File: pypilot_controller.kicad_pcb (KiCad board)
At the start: 4 copper layers, 76.6 x 50.6 mm, 99 parts, among them J1 power+, J10 Clutch, J2 power-, J3 Motor A, J4 Motor B, J5 UART_Device, J6 Rudder, J7 End Stops, J8 Conn_01x02, J9 ISP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

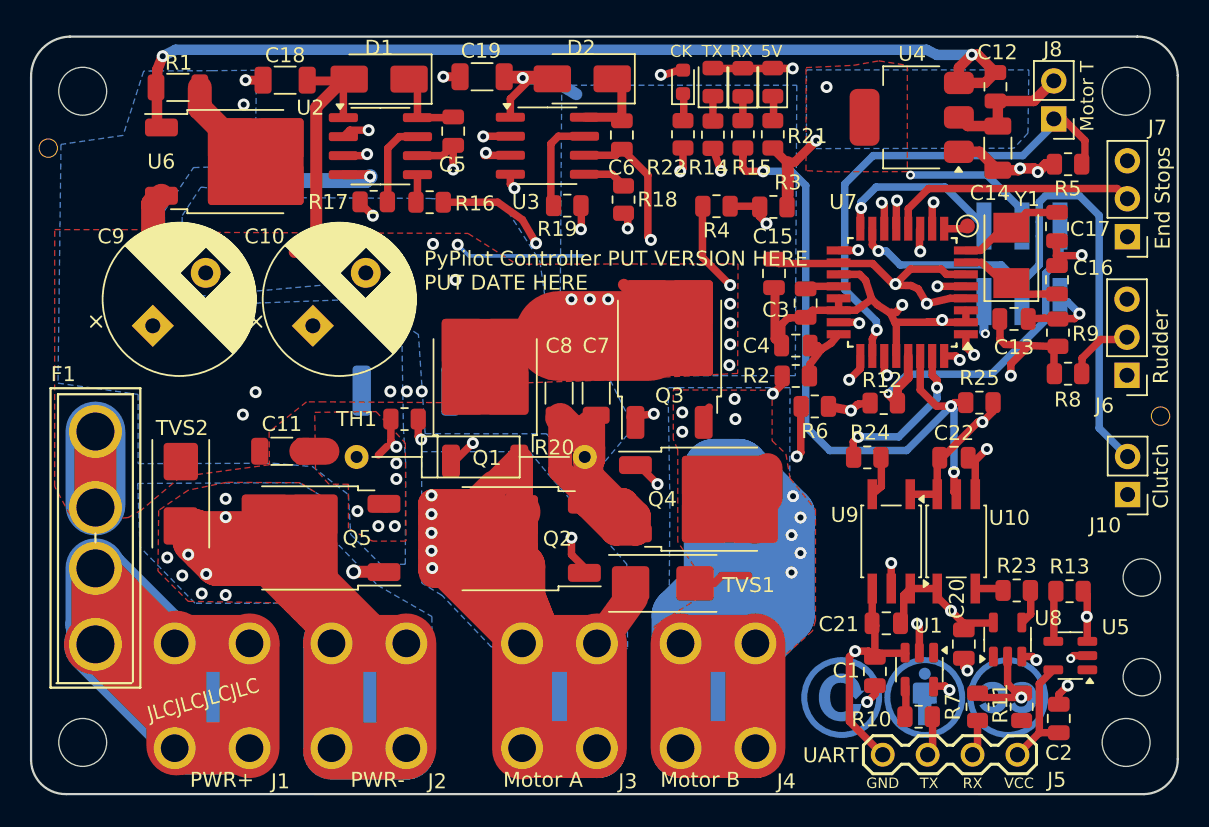
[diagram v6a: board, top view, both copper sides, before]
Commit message: Track cleanups, mostly from Tools -> Cleanup Tracks & Vias
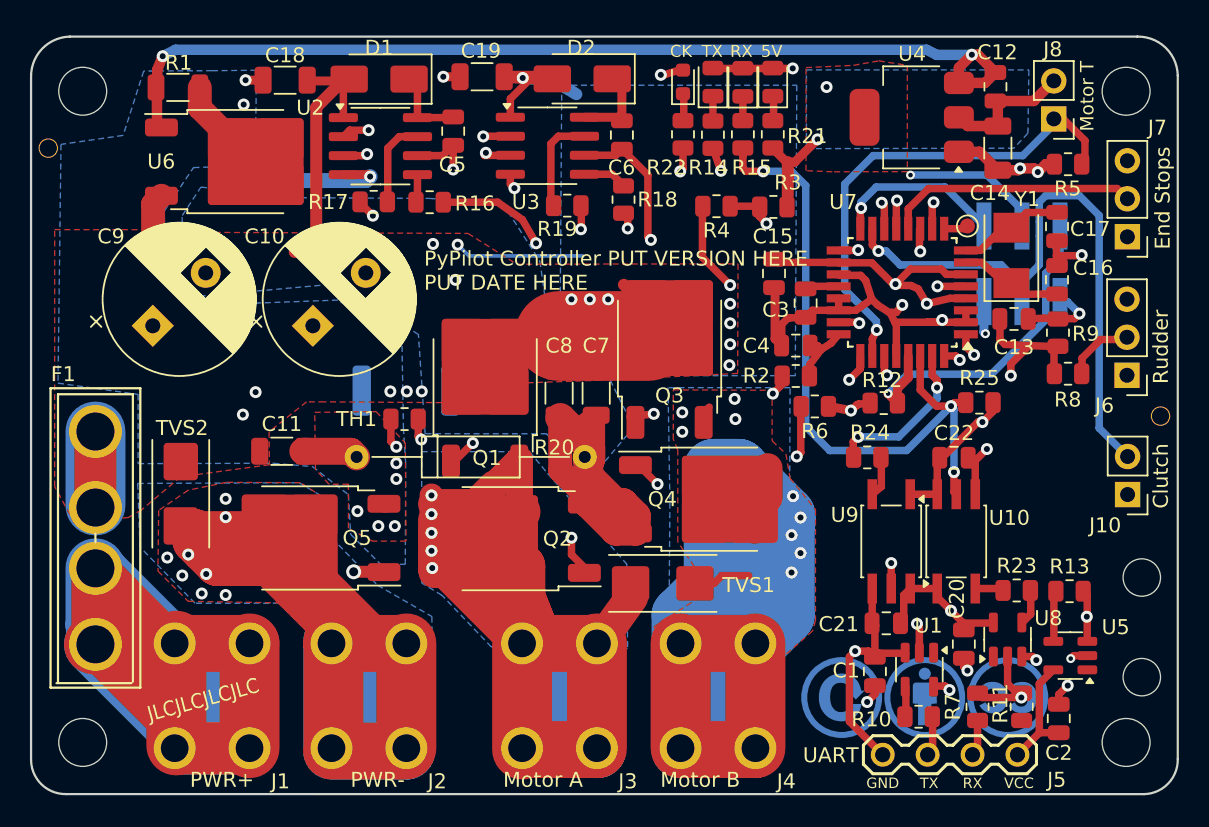
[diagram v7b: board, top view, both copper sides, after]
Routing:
- net Net-(J3-Pin_1): track 162.2 -> 166.1 mm
- net GND: track 82.6 -> 84.1 mm
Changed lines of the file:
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@@
 	)
 	(segment
-		(start 25.618763 28.331237)
-		(end 25.05 28.9)
-		(width 0.5)
-		(layer "F.Cu")
-		(net 1)
-	)
-	(segment
 		(start 55.7974 19.232)
 		(end 55.7974 18.432)
@@
 	)
 	(segment
+		(start 57.2654 16.9)
+		(end 57.5974 17.232)
+		(width 0.5)
+		(layer "F.Cu")
+		(net 1)
+	)
+	(segment
 		(start 51.3988 8.4154)
 		(end 52.3154 9.332)
@@
 	)
 	(segment
-		(start 20 28.65)
-		(end 21.55 28.65)
-		(width 1.8)
-		(layer "F.Cu")
-		(net 1)
-	)
-	(segment
 		(start 69.5198 19.7612)
 		(end 70.4474 19.7889)
@@
 	)
 	(segment
+		(start 23.2166 28.65)
+		(end 23.5966 29.03)
+		(width 1.8)
+		(layer "F.Cu")
+		(net 1)
+	)
+	(segment
 		(start 64.9224 29.2776)
 		(end 65.7 28.5)
@@
 	)
 	(segment
+		(start 52.3154 9.332)
+		(end 52.868 9.332)
+		(width 0.6)
+		(layer "F.Cu")
+		(net 1)
+	)
+	(segment
 		(start 70.3474 14.611)
 		(end 70.3834 14.575)
@@
 	)
 	(segment
+		(start 55.7974 16.832)
+		(end 55.8654 16.9)
+		(width 0.5)
+		(layer "F.Cu")
+		(net 1)
+	)
+	(segment
 		(start 68.8286 5.25)
 		(end 70.1698 3.9088)
@@
 	)
 	(segment
+		(start 55.8654 16.9)
+		(end 57.2654 16.9)
+		(width 0.5)
+		(layer "F.Cu")
+		(net 1)
+	)
+	(segment
 		(start 33.8662 10.1456)
 		(end 33.8662 10.803)
@@
 	)
 	(segment
-		(start 70.3474 16.256)
-		(end 70.3474 15.585)
-		(width 0.5)
+		(start 20 28.65)
+		(end 23.2166 28.65)
+		(width 1.8)
 		(layer "F.Cu")
 		(net 1)
 	)
 	(segment
-		(start 52.3154 9.332)
-		(end 52.868 9.332)
-		(width 0.6)
+		(start 70.3474 16.256)
+		(end 70.3474 15.585)
+		(width 0.5)
 		(layer "F.Cu")
 		(net 1)
@@
 	)
 	(segment
-		(start 52.868 9.332)
-		(end 54.3 7.9)
-		(width 0.6)
-		(layer "F.Cu")
-		(net 1)
-	)
-	(segment
 		(start 33.8662 10.803)
 		(end 34.1376 11.0744)
@@
 	)
 	(segment
-		(start 57.1974 16.832)
-		(end 57.5974 17.232)
-		(width 0.5)
-		(layer "F.Cu")
-		(net 1)
-	)
-	(segment
 		(start 51.9984 20.163)
 		(end 51.9984 21.59)
@@
 	)
 	(segment
-		(start 57.5974 17.232)
-		(end 58.0099 18.4945)
-		(width 0.5)
-		(layer "F.Cu")
-		(net 1)
-	)
-	(segment
 		(start 52.3736 12.2186)
 		(end 52.4002 12.192)
@@
 	)
 	(segment
+		(start 57.5974 17.232)
+		(end 58.0099 18.4945)
+		(width 0.5)
+		(layer "F.Cu")
+		(net 1)
+	)
+	(segment
 		(start 58.3784 18.863)
 		(end 58.0099 18.4945)
@@
 	)
 	(segment
-		(start 55.7974 16.832)
-		(end 57.1974 16.832)
-		(width 0.5)
-		(layer "F.Cu")
-		(net 1)
-	)
-	(segment
 		(start 25.8875 26.5)
 		(end 25.8875 27.9875)
@@
 	)
 	(segment
+		(start 52.868 9.332)
+		(end 54.386397 7.813603)
+		(width 0.6)
+		(layer "F.Cu")
+		(net 1)
+	)
+	(segment
 		(start 52.3974 9.332)
 		(end 52.4002 10.3378)
@@
 	)
 	(via
-		(at 54.3 7.9)
+		(at 54.386397 7.813603)
 		(size 0.8)
 		(drill 0.4)
@@
 	)
 	(segment
-		(start 25.45 36.855)
-		(end 25.295 36.7)
-		(width 0.8)
-		(layer "F.Cu")
-		(net 2)
-	)
-	(segment
 		(start 36.5356 3.6356)
 		(end 36.67 3.77)
@@
 	)
 	(segment
-		(start 33.3786 3.6322)
-		(end 33.4484 3.6356)
-		(width 0.8)
-		(layer "F.Cu")
-		(net 2)
-	)
-	(segment
 		(start 36.6044 3.8356)
 		(end 35.1348 3.8356)
@@
 	)
 	(segment
-		(start 28.75 36.775)
-		(end 28.75 36.775)
-		(width 2)
-		(layer "F.Cu")
-		(net 21)
-	)
-	(segment
 		(start 28.7 35.525)
 		(end 28.7 34.325)
@@
 	)
 	(segment
-		(start 28.7 33.225)
-		(end 28.7 32.175)
-		(width 2)
-		(layer "F.Cu")
-		(net 21)
-	)
-	(segment
-		(start 28.7 32.175)
-		(end 28.7 32.175)
-		(width 2)
-		(layer "F.Cu")
-		(net 21)
-	)
-	(segment
 		(start 28.7 32.175)
 		(end 31.53 32.175)
@@
 	)
 	(segment
+		(start 28.6 36.4)
+		(end 28.65 36.45)
+		(width 1.6)
+		(layer "F.Cu")
+		(net 21)
+	)
+	(segment
+		(start 28.6 31.6)
+		(end 28.6 36.4)
+		(width 1.6)
+		(layer "F.Cu")
+		(net 21)
+	)
+	(segment
 		(start 27.6614 8.901)
 		(end 29.3491 8.901)
@@
 	(segment
 		(start 30.0482 9.8298)
-		(end 30.0482 9.1694)
-		(width 0.5)
-		(layer "F.Cu")
-		(net 21)
-	)
-	(segment
-		(start 30.0482 9.1694)
 		(end 30.0482 8.2019)
 		(width 0.5)
@@
 	)
 	(segment
-		(start 32.0548 7.62)
-		(end 50.8254 7.62)
+		(start 52.92 7.62)
+		(end 56.281999 10.981999)
 		(width 0.5)
 		(layer "In2.Cu")
@@
 	)
 	(segment
-		(start 58.674796 11.974868)
+		(start 57.612148 10.981999)
 		(end 58.674796 12.044647)
 		(width 0.5)
@@
 	)
 	(segment
-		(start 57.681927 10.981999)
-		(end 58.674796 11.974868)
-		(width 0.5)
-		(layer "In2.Cu")
-		(net 23)
-	)
-	(segment
-		(start 50.8254 7.62)
-		(end 55.305401 10.981999)
+		(start 32.0548 7.62)
+		(end 52.92 7.62)
 		(width 0.5)
 		(layer "In2.Cu")
@@
 	)
 	(segment
-		(start 55.305401 10.981999)
-		(end 57.681927 10.981999)
+		(start 56.281999 10.981999)
+		(end 57.612148 10.981999)
 		(width 0.5)
 		(layer "In2.Cu")
@@
 	)
 	(segment
-		(start 50.8508 13.5636)
-		(end 50.9778 13.4366)
-		(width 0.5)
-		(layer "B.Cu")
-		(net 24)
-	)
-	(segment
 		(start 27.7125 27.6617)
 		(end 27.9146 27.8638)
@@
 	)
 	(segment
-		(start 52.2 39.575)
-		(end 52.2 39.575)
-		(width 4)
-		(layer "B.Cu")
-		(net 26)
-	)
-	(segment
 		(start 52.25 33.377)
 		(end 52.25 32.973002)
@@
 	)
 	(segment
+		(start 51.694 16.034)
+		(end 55.7956 16.034)
+		(width 0.5)
+		(layer "F.Cu")
+		(net 28)
+	)
+	(segment
 		(start 63.829 8.6442)
 		(end 65.1992 8.6442)
@@
 	)
 	(segment
-		(start 58.060396 16.109)
-		(end 51.7994 16.109)
-		(width 0.5)
-		(layer "F.Cu")
-		(net 28)
-	)
-	(segment
 		(start 56.6166 25.9334)
 		(end 55.1434 25.654)
@@
 	)
 	(segment
+		(start 55.822312 16.060712)
+		(end 58.012108 16.060712)
+		(width 0.5)
+		(layer "F.Cu")
+		(net 28)
+	)
+	(segment
+		(start 58.012108 16.060712)
+		(end 59.515398 17.564002)
+		(width 0.5)
+		(layer "F.Cu")
+		(net 28)
+	)
+	(segment
 		(start 57.016599 25.533401)
 		(end 57.092799 25.533401)
@@
 	)
 	(segment
-		(start 51.7994 16.109)
-		(end 51.5474 15.857)
-		(width 0.5)
-		(layer "F.Cu")
-		(net 28)
-	)
-	(segment
 		(start 56.6166 25.9334)
 		(end 57.016599 25.533401)
@@
 	)
 	(segment
-		(start 59.515398 17.564002)
-		(end 58.060396 16.109)
+		(start 51.48 15.82)
+		(end 51.694 16.034)
 		(width 0.5)
 		(layer "F.Cu")
@@
 	)
 	(segment
+		(start 55.7956 16.034)
+		(end 55.822312 16.060712)
+		(width 0.5)
+		(layer "F.Cu")
+		(net 28)
+	)
+	(segment
 		(start 62.6474 16.482)
 		(end 60.5974 16.482)
@@
 		(end 14.3 36.15)
 		(width 3)
-		(layer "F.Cu")
-		(net 33)
-	)
-	(segment
-		(start 14.3 36.15)
-		(end 14.3 36.15)
-		(width 3)

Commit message: Cleaned LCSC part numbers out of datasheet field (and renamed 0.1u to 100n)
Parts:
- C13, C15, C3, C4: value .1uF -> 100n
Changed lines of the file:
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@@
 			)
 		)
-		(property "Datasheet" "C468907"
+		(property "Datasheet" ""
 			(at 0.64944 0 180)
 			(unlocked yes)
@@
 			)
 		)
-		(property "LCSC" "C83327"
+		(property "LCSC" "*C83327, C468907 "
 			(at 0 0 180)
 			(unlocked yes)
@@
 			)
 		)
-		(property "Datasheet" "C51597, C72672"
+		(property "Datasheet" ""
 			(at 0 0 180)
 			(unlocked yes)
@@
 			)
 		)
-		(property "LCSC" "C72672"
+		(property "LCSC" "*C72672, C51597"
 			(at 0 0 180)
 			(unlocked yes)
@@
 			)
 		)
-		(property "Value" ".1uF"
+		(property "Value" "100n"
 			(at 0 1.65 90)
 			(layer "F.Fab")
@@
 			)
 		)
-		(property "Value" ".1uF"
+		(property "Value" "100n"
 			(at 0 1.65 90)
 			(layer "F.Fab")
@@
 			)
 		)
-		(property "Value" ".1uF"
+		(property "Value" "100n"
 			(at 0 1.65 0)
 			(layer "F.Fab")
@@
 			)
 		)
-		(property "Value" ".1uF"
+		(property "Value" "100n"
 			(at 0 1.65 0)
 			(layer "F.Fab")
@@
 			)
 		)
+		(property "LCSC" "C49678"
+			(at 0 0 180)
+			(unlocked yes)
+			(layer "F.Fab")
+			(hide yes)
+			(effects
+				(font
+					(size 1 1)
+					(thickness 0.15)
+				)
+			)
+		)
 		(property ki_fp_filters "C_*")
 		(sheetname "opto")
@@
 			)
 		)
-		(property "Datasheet" "C283478"
+		(property "Datasheet" ""
 			(at 0.64944 0 90)
 			(unlocked yes)
@@
 			)
 		)
-		(property "LCSC" "C83327"
+		(property "LCSC" "*C83327, C283478"
 			(at 0 0 90)
 			(unlocked yes)
